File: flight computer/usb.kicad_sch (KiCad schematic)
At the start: 33 parts, among them J11 USB_C_Receptacle_USB2.0_16P, J23 USB_C_Receptacle_USB2.0_16P, J24 USB_C_Receptacle_USB2.0_16P

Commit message: tspmo
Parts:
- removed C37, C39: 4n7, Capacitor_SMD:C_0603_1608Metric, symbol Device:C
- removed C38, C40: 100n, Capacitor_SMD:C_0603_1608Metric, symbol Device:C
- removed D10, D12: PRTR5V0U2X, Package_TO_SOT_SMD:SOT-143, symbol Power_Protection:PRTR5V0U2X
- removed D11, D9: LED, LED_SMD:LED_0603_1608Metric, symbol Device:LED
- removed D27, D28: PMEG6020ER, Diode_SMD:Nexperia_CFP3_SOD-123W, symbol Diode:PMEG6020ER
- removed J23, J24: USB_C_Receptacle_USB2.0_16P, Connector_USB:USB_C_Receptacle_GCT_USB4105-xx-A_16P_TopMnt_Horizontal, symbol Connector:USB_C_Receptacle_USB2.0_16P
- removed R48, R49, R86, R96: 5k1, Resistor_SMD:R_0603_1608Metric, symbol Device:R
- removed R50, R97: 330, Resistor_SMD:R_0603_1608Metric, symbol Device:R
- removed TP14, TP15, TP16, TP17: TestPoint, TestPoint:TestPoint_Pad_1.0x1.0mm, symbol Connector:TestPoint
- added SW1, SW2: SW_SP3T, NR01103ANG13-1C:SW_NR01103ANG13-1C, symbol Switch:SW_SP3T
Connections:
- net D+ DMCU-1: now also SW1.2
- net D+ DMCU-2: now also SW1.4
- net D+ MMCU: now also SW1.1; no longer D8.2 (I/O1), J11.A6 (D+), J11.B6 (D+), TP12.1
- net D- DMCU-1: now also SW2.2
- net D- DMCU-2: now also SW2.4
- net D- MMCU: now also SW2.1; no longer D8.3 (I/O2), J11.A7 (D-), J11.B7 (D-), TP13.1
- new net: D8.3 (I/O2), J11.A7 (D-), J11.B7 (D-), SW2.3, TP13.1
- new net: D8.2 (I/O1), J11.A6 (D+), J11.B6 (D+), SW1.3, TP12.1
- no-connect marks 6 -> 2

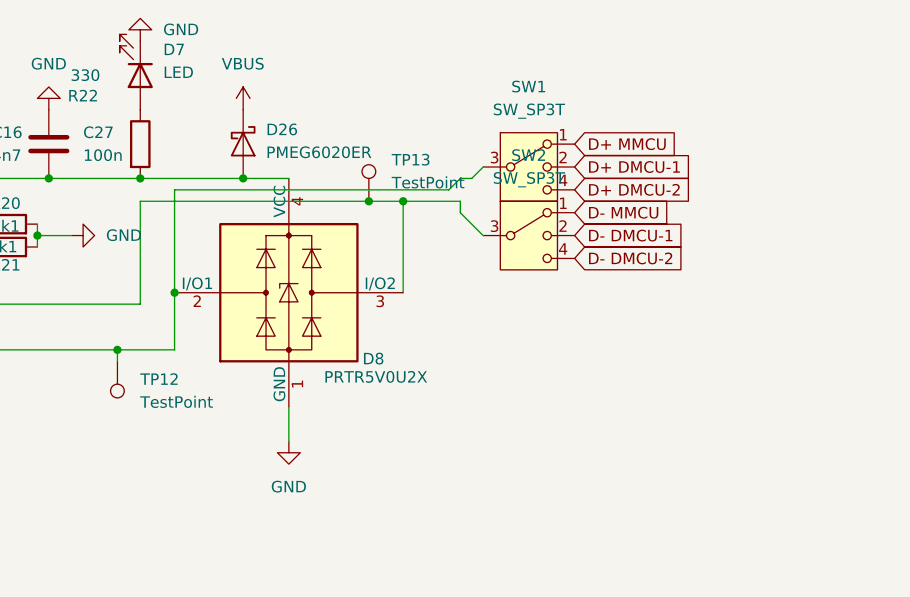
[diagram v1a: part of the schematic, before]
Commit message: started to change to bridging and PCB stiching and stuff fixes
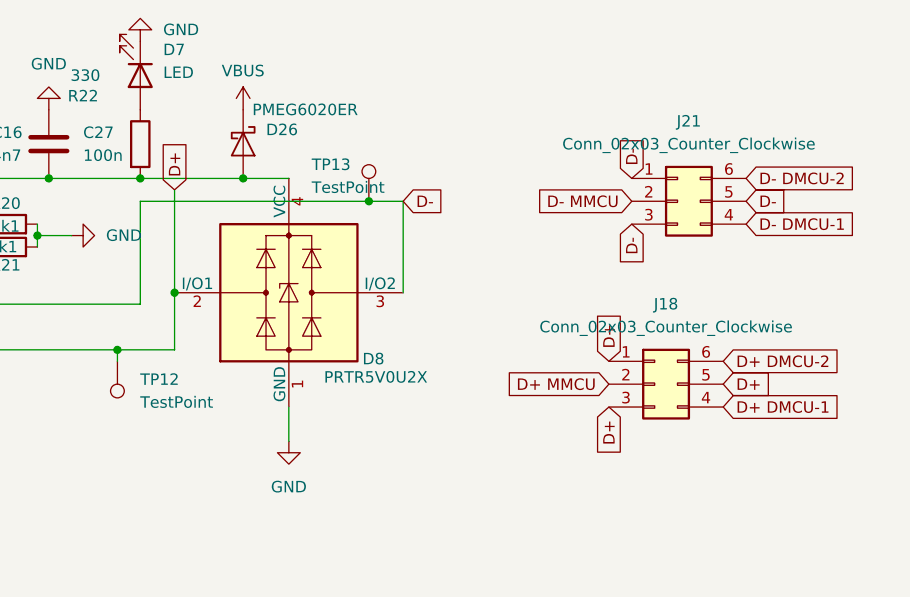
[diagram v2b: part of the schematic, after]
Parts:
- removed SW1, SW2: SW_SP3T, NR01103ANG13-1C:SW_NR01103ANG13-1C, symbol Switch:SW_SP3T
- added J18, J21: Conn_02x03_Counter_Clockwise, symbol Connector_Generic:Conn_02x03_Counter_Clockwise
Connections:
- net D+ DMCU-1: now also J18.4 (Pin_4)
- net D+ DMCU-2: now also J18.6 (Pin_6)
- net D+ MMCU: now also J18.2 (Pin_2)
- net D- DMCU-1: now also J21.4 (Pin_4)
- net D- DMCU-2: now also J21.6 (Pin_6)
- net D- MMCU: now also J21.2 (Pin_2)
- net D-: now reaches D8.3 (I/O2), J11.A7 (D-), J11.B7 (D-), TP13.1
- net D-: now also J21.1 (Pin_1), J21.3 (Pin_3), J21.5 (Pin_5)
- net D+  : now reaches D8.2 (I/O1), J11.A6 (D+), J11.B6 (D+), TP12.1
- net D+  : now also J18.1 (Pin_1), J18.3 (Pin_3), J18.5 (Pin_5)

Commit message: Wired the headers for programming 3 MCU'S + some footprint fixes and additions for photos:(
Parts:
- J18, J21: footprint (none) -> Connector_PinSocket_2.00mm:PinSocket_2x03_P2.00mm_Horizontal
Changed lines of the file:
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@@
 			)
 		)
-		(property "Footprint" ""
+		(property "Footprint" "Connector_PinSocket_2.00mm:PinSocket_2x03_P2.00mm_Horizontal"
 			(at 127 30.48 0)
 			(effects
@@
 			)
 		)
-		(property "Footprint" ""
+		(property "Footprint" "Connector_PinSocket_2.00mm:PinSocket_2x03_P2.00mm_Horizontal"
 			(at 124.46 50.8 0)
 			(effects

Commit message: Meddy, the PCB is ready for you. The proper RF is setup too on the PCB
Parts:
- added FB1: BLM18AG601SN1D, Resistor_SMD:R_0603_1608Metric, symbol Device:FerriteBead_Small
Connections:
- net GND: now also FB1.2; no longer J11.S1 (SHIELD)
- new net: FB1.1, J11.S1 (SHIELD)
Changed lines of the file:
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@@
 	(paper "A4")
+	(junction
+		(at 27.94 66.04)
+		(diameter 0)
+		(color 0 0 0 0)
+	)
 	(junction
 		(at 43.18 46.99)
@@
 	(wire
 		(pts
+			(xy 26.67 66.04) (xy 27.94 66.04)
+		)
+		(stroke
+			(width 0)
+			(type default)
+		)
+	)
+	(wire
+		(pts
 			(xy 55.88 33.02) (xy 55.88 34.29)
 		)
@@
 		(pts
 			(xy 67.31 27.94) (xy 78.74 27.94)
+		)
+		(stroke
+			(width 0)
+			(type default)
+		)
+	)
+	(wire
+		(pts
+			(xy 21.59 66.04) (xy 20.32 66.04)
 		)
 		(stroke
@@
 	(symbol
 		(lib_id "power:GND")
-		(at 20.32 66.04 0)
-		(unit 1)
-		(exclude_from_sim no)
-		(in_bom yes)
-		(on_board yes)
-		(dnp no)
-		(property "Reference" "#PWR070"
-			(at 20.32 72.39 0)
-			(effects
-				(font
-					(size 1.27 1.27)
-				)
-				(hide yes)
-			)
-		)
-		(property "Value" "GND"
-			(at 20.32 71.12 0)
-			(effects
-				(font
-					(size 1.27 1.27)
-				)
-			)
-		)
-		(property "Footprint" ""
-			(at 20.32 66.04 0)
-			(effects
-				(font
-					(size 1.27 1.27)
-				)
-				(hide yes)
-			)
-		)
-		(property "Datasheet" ""
-			(at 20.32 66.04 0)
-			(effects
-				(font
-					(size 1.27 1.27)
-				)
-				(hide yes)
-			)
-		)
-		(property "Description" "Power symbol creates a global label with name \"GND\" , ground"
-			(at 20.32 66.04 0)
-			(effects
-				(font
-					(size 1.27 1.27)
-				)
-				(hide yes)
-			)
-		)
-		(pin "1"
-		)
-		(instances
-			(project "horizon"
-				(path "/78d9c2f3-deae-418a-8c21-4820ea8fc57f/097de61a-b781-409b-916d-2a6fba459f37"
-					(reference "#PWR070")
-					(unit 1)
-				)
-			)
-		)
-	)
-	(symbol
-		(lib_id "power:GND")
 		(at 57.15 20.32 180)
 		(unit 1)
@@
 	)
 	(symbol
-		(lib_id "power:GND")
-		(at 27.94 66.04 0)
+		(lib_id "Device:FerriteBead_Small")
+		(at 24.13 66.04 90)
 		(unit 1)
 		(exclude_from_sim no)
@@
 		(on_board yes)
 		(dnp no)
-		(fields_autoplaced yes)
-		(property "Reference" "#PWR0154"
-			(at 27.94 72.39 0)
-			(effects
-				(font
-					(size 1.27 1.27)
-				)
-				(hide yes)
-			)
-		)
-		(property "Value" "GND"
-			(at 27.94 71.12 0)
-			(effects
-				(font
-					(size 1.27 1.27)
-				)
-			)
-		)
-		(property "Footprint" ""
-			(at 27.94 66.04 0)
-			(effects
-				(font
-					(size 1.27 1.27)
-				)
-				(hide yes)
-			)
-		)
-		(property "Datasheet" ""
-			(at 27.94 66.04 0)
-			(effects
-				(font
-					(size 1.27 1.27)
-				)
-				(hide yes)
-			)
-		)
-		(property "Description" "Power symbol creates a global label with name \"GND\" , ground"
-			(at 27.94 66.04 0)
-			(effects
-				(font
-					(size 1.27 1.27)
-				)
-				(hide yes)
-			)
+		(property "Reference" "FB1"
+			(at 24.13 70.104 90)
+			(effects
+				(font
+					(size 1.27 1.27)
+				)
+			)
+		)
+		(property "Value" "BLM18AG601SN1D"
+			(at 24.13 72.644 90)
+			(effects
+				(font
+					(size 1.27 1.27)
+				)
+			)
+		)
+		(property "Footprint" "Resistor_SMD:R_0603_1608Metric"
+			(at 24.13 67.818 90)
+			(effects
+				(font
+					(size 1.27 1.27)
+				)
+				(hide yes)
+			)
+		)
+		(property "Datasheet" "~"
+			(at 24.13 66.04 0)
+			(effects
+				(font
+					(size 1.27 1.27)
+				)
+				(hide yes)
+			)
+		)
+		(property "Description" "Ferrite bead, small symbol"
+			(at 24.13 66.04 0)
+			(effects
+				(font
+					(size 1.27 1.27)
+				)
+				(hide yes)
+			)
+		)
+		(property "LCSC Part" "C19330"
+			(at 24.13 66.04 0)
+			(effects
+				(font
+					(size 1.27 1.27)
+				)
+				(hide yes)
+			)
+		)
+		(pin "2"
 		)
 		(pin "1"
@@
 			(project "horizon"
 				(path "/78d9c2f3-deae-418a-8c21-4820ea8fc57f/097de61a-b781-409b-916d-2a6fba459f37"
-					(reference "#PWR0154")
+					(reference "FB1")
 					(unit 1)
 				)
@@
 					(unit 1)
 				)
+			)
+		)
+	)
+	(symbol
+		(lib_id "power:GND")
+		(at 27.94 66.04 0)
+		(unit 1)
+		(exclude_from_sim no)
+		(in_bom yes)
+		(on_board yes)
+		(dnp no)
+		(property "Reference" "#PWR033"
+			(at 27.94 72.39 0)
+			(effects
+				(font
+					(size 1.27 1.27)
+				)
+				(hide yes)
+			)
+		)
+		(property "Value" "GND"
+			(at 27.94 71.12 0)
+			(effects
+				(font
+					(size 1.27 1.27)
+				)
+			)
+		)
+		(property "Footprint" ""
+			(at 27.94 66.04 0)
+			(effects
+				(font
+					(size 1.27 1.27)
+				)
+				(hide yes)
+			)
+		)
+		(property "Datasheet" ""
+			(at 27.94 66.04 0)
+			(effects
+				(font
+					(size 1.27 1.27)
+				)
+				(hide yes)
+			)
+		)
+		(property "Description" "Power symbol creates a global label with name \"GND\" , ground"
+			(at 27.94 66.04 0)
+			(effects
+				(font
+					(size 1.27 1.27)
+				)
+				(hide yes)
+			)
+		)
+		(pin "1"
+		)
+		(instances
+			(project "horizon"
+				(path "/78d9c2f3-deae-418a-8c21-4820ea8fc57f/097de61a-b781-409b-916d-2a6fba459f37"
+					(reference "#PWR033")
+					(unit 1)
+				)

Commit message: finished power stuff
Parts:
- removed TP12, TP13: TestPoint, TestPoint:TestPoint_Pad_1.0x1.0mm, symbol Connector:TestPoint
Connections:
- net D-: now also D8.2 (I/O1); no longer D8.3 (I/O2)
- net D+   renamed D+
- net D+: now also D8.3 (I/O2); no longer D8.2 (I/O1)
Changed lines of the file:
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@@
-	)
-	(junction
-		(at 64.77 46.99)
-		(diameter 0)
-		(color 0 0 0 0)
 	)
 	(junction
@@
 	)
 	(junction
-		(at 92.71 30.48)
-		(diameter 0)
-		(color 0 0 0 0)
-	)
-	(junction
-		(at 71.12 40.64)
-		(diameter 0)
-		(color 0 0 0 0)
-	)
-	(junction
 		(at 78.74 27.94)
 		(diameter 0)
@@
 	(wire
 		(pts
+			(xy 68.58 29.21) (xy 95.25 29.21)
+		)
+		(stroke
+			(width 0)
+			(type default)
+		)
+	)
+	(wire
+		(pts
 			(xy 55.88 34.29) (xy 59.69 34.29)
 		)
@@
 	(wire
 		(pts
-			(xy 71.12 40.64) (xy 71.12 29.21)
-		)
-		(stroke
-			(width 0)
-			(type default)
-		)
-	)
-	(wire
-		(pts
-			(xy 92.71 30.48) (xy 96.52 30.48)
+			(xy 68.58 29.21) (xy 68.58 46.99)
+		)
+		(stroke
+			(width 0)
+			(type default)
+		)
+	)
+	(wire
+		(pts
+			(xy 67.31 30.48) (xy 96.52 30.48)
 		)
 		(stroke
@@
 	(wire
 		(pts
-			(xy 43.18 46.99) (xy 64.77 46.99)
-		)
-		(stroke
-			(width 0)
-			(type default)
-		)
-	)
-	(wire
-		(pts
 			(xy 43.18 27.94) (xy 46.99 27.94)
 		)
@@
 	(wire
 		(pts
-			(xy 67.31 30.48) (xy 92.71 30.48)
-		)
-		(stroke
-			(width 0)
-			(type default)
-		)
-	)
-	(wire
-		(pts
 			(xy 46.99 27.94) (xy 57.15 27.94)
 		)
@@
 	(wire
 		(pts
-			(xy 64.77 48.26) (xy 64.77 46.99)
-		)
-		(stroke
-			(width 0)
-			(type default)
-		)
-	)
-	(wire
-		(pts
-			(xy 71.12 46.99) (xy 71.12 40.64)
-		)
-		(stroke
-			(width 0)
-			(type default)
-		)
-	)
-	(wire
-		(pts
-			(xy 96.52 30.48) (xy 96.52 40.64)
-		)
-		(stroke
-			(width 0)
-			(type default)
-		)
-	)
-	(wire
-		(pts
-			(xy 64.77 46.99) (xy 71.12 46.99)
+			(xy 43.18 46.99) (xy 68.58 46.99)
 		)
 		(stroke
@@
 		(pts
 			(xy 43.18 46.99) (xy 43.18 48.26)
+		)
+		(stroke
+			(width 0)
+			(type default)
+		)
+	)
+	(wire
+		(pts
+			(xy 95.25 29.21) (xy 96.52 27.94)
 		)
 		(stroke
@@
 		)
 	)
+	(global_label "D+"
+		(shape input)
+		(at 96.52 27.94 0)
+		(fields_autoplaced yes)
+		(effects
+			(font
+				(size 1.27 1.27)
+			)
+			(justify left)
+		)
+		(property "Intersheetrefs" "${INTERSHEET_REFS}"
+			(at 102.3476 27.94 0)
+			(effects
+				(font
+					(size 1.27 1.27)
+				)
+				(justify left)
+				(hide yes)
+			)
+		)
+	)
 	(global_label "D- DMCU-1"
 		(shape input)
@@
 		)
 	)
+	(global_label "D-"
+		(shape input)
+		(at 71.12 40.64 180)
+		(fields_autoplaced yes)
+		(effects
+			(font
+				(size 1.27 1.27)
+			)
+			(justify right)
+		)
+		(property "Intersheetrefs" "${INTERSHEET_REFS}"
+			(at 65.2924 40.64 0)
+			(effects
+				(font
+					(size 1.27 1.27)
+				)
+				(justify right)
+				(hide yes)
+			)
+		)
+	)
+	(global_label "D+"
+		(shape input)
+		(at 96.52 40.64 0)
+		(fields_autoplaced yes)
+		(effects
+			(font
+				(size 1.27 1.27)
+			)
+			(justify left)
+		)
+		(property "Intersheetrefs" "${INTERSHEET_REFS}"
+			(at 102.3476 40.64 0)
+			(effects
+				(font
+					(size 1.27 1.27)
+				)
+				(justify left)
+				(hide yes)
+			)
+		)
+	)
 	(global_label "D+ DMCU-2"
 		(shape input)
@@
 		)
 	)
-	(global_label "D+  "
+	(global_label "D+"
 		(shape input)
 		(at 132.08 50.8 0)
@@
 		)
 		(property "Intersheetrefs" "${INTERSHEET_REFS}"
-			(at 139.8428 50.8 0)
+			(at 137.9076 50.8 0)
 			(effects
 				(font
@@
 		)
 	)
-	(global_label "D+  "
+	(global_label "D+"
 		(shape input)
 		(at 119.38 48.26 90)
@@
 		)
 		(property "Intersheetrefs" "${INTERSHEET_REFS}"
-			(at 119.38 40.4972 90)
+			(at 119.38 42.4324 90)
 			(effects
 				(font
@@
 		)
 	)
-	(global_label "D+  "
+	(global_label "D+"
 		(shape input)
-		(at 71.12 29.21 90)
+		(at 119.38 53.34 270)
 		(fields_autoplaced yes)
 		(effects
@@
 				(size 1.27 1.27)
 			)
-			(justify left)
+			(justify right)
 		)
 		(property "Intersheetrefs" "${INTERSHEET_REFS}"
-			(at 71.12 21.4472 90)
-			(effects
-				(font
-					(size 1.27 1.27)
-				)
-				(justify left)
-				(hide yes)
-			)
-		)
-	)
-	(global_label "D+  "
-		(shape input)
-		(at 119.38 53.34 270)
-		(fields_autoplaced yes)
-		(effects
-			(font
-				(size 1.27 1.27)
-			)
-			(justify right)
-		)
-		(property "Intersheetrefs" "${INTERSHEET_REFS}"
-			(at 119.38 61.1028 90)
+			(at 119.38 59.1676 90)
 			(effects
 				(font
@@
 	)
 	(symbol
-		(lib_id "Connector:TestPoint")
-		(at 64.77 48.26 180)
-		(unit 1)
-		(exclude_from_sim no)
-		(in_bom yes)
-		(on_board yes)
-		(dnp no)
-		(fields_autoplaced yes)
-		(property "Reference" "TP12"
-			(at 67.31 50.2919 0)
-			(effects
-				(font
-					(size 1.27 1.27)
-				)
-				(justify right)
-			)
-		)
-		(property "Value" "TestPoint"
-			(at 67.31 52.8319 0)
-			(effects
-				(font
-					(size 1.27 1.27)
-				)
-				(justify right)
-			)
-		)
-		(property "Footprint" "TestPoint:TestPoint_Pad_1.0x1.0mm"
-			(at 59.69 48.26 0)
-			(effects
-				(font
-					(size 1.27 1.27)
-				)
-				(hide yes)
-			)
-		)
-		(property "Datasheet" "~"
-			(at 59.69 48.26 0)
-			(effects
-				(font
-					(size 1.27 1.27)
-				)
-				(hide yes)
-			)
-		)
-		(property "Description" "test point"
-			(at 64.77 48.26 0)
-			(effects
-				(font
-					(size 1.27 1.27)
-				)
-				(hide yes)
-			)
-		)
-		(pin "1"
-		)
-		(instances
-			(project "horizon"
-				(path "/78d9c2f3-deae-418a-8c21-4820ea8fc57f/097de61a-b781-409b-916d-2a6fba459f37"
-					(reference "TP12")
-					(unit 1)
-				)
-			)
-		)
-	)
-	(symbol
 		(lib_id "Device:R")
 		(at 52.07 33.02 90)
@@
 					(unit 1)
 				)
-			)
-		)
-	)
-	(symbol
-		(lib_id "Connector:TestPoint")
-		(at 92.71 30.48 0)
-		(unit 1)
-		(exclude_from_sim no)
-		(in_bom yes)
-		(on_board yes)
-		(dnp no)
-		(property "Reference" "TP13"
-			(at 86.36 26.416 0)
-			(effects
-				(font
-					(size 1.27 1.27)
-				)
-				(justify left)
-			)
-		)
-		(property "Value" "TestPoint"
-			(at 86.36 28.956 0)
-			(effects
-				(font
-					(size 1.27 1.27)
-				)
-				(justify left)
-			)
-		)
-		(property "Footprint" "TestPoint:TestPoint_Pad_1.0x1.0mm"
-			(at 97.79 30.48 0)
-			(effects
-				(font
-					(size 1.27 1.27)
-				)
-				(hide yes)
-			)
-		)
-		(property "Datasheet" "~"
-			(at 97.79 30.48 0)
-			(effects
-				(font
-					(size 1.27 1.27)
-				)
-				(hide yes)
-			)
-		)
-		(property "Description" "test point"
-			(at 92.71 30.48 0)
-			(effects
-				(font
-					(size 1.27 1.27)
-				)
-				(hide yes)
-			)
-		)
-		(pin "1"
-		)
-		(instances
-			(project "horizon"
-				(path "/78d9c2f3-deae-418a-8c21-4820ea8fc57f/097de61a-b781-409b-916d-2a6fba459f37"
-					(reference "TP13")
-					(unit 1)
-				)

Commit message: wiirng
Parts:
- J18, J21: footprint Connector_PinSocket_2.00mm:PinSocket_2x03_P2.00mm_Horizontal -> Connector_PinHeader_1.00mm:PinHeader_2x03_P1.00mm_Vertical
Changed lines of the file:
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@@
 			)
 		)
-		(property "Footprint" "Connector_PinSocket_2.00mm:PinSocket_2x03_P2.00mm_Horizontal"
+		(property "Footprint" "Connector_PinHeader_1.00mm:PinHeader_2x03_P1.00mm_Vertical"
 			(at 127 30.48 0)
 			(effects
@@
 			)
 		)
-		(property "Footprint" "Connector_PinSocket_2.00mm:PinSocket_2x03_P2.00mm_Horizontal"
+		(property "Footprint" "Connector_PinHeader_1.00mm:PinHeader_2x03_P1.00mm_Vertical"
 			(at 124.46 50.8 0)
 			(effects

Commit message: started newest layout + wiring
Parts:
- removed FB1: BLM18AG601SN1D, Resistor_SMD:R_0603_1608Metric, symbol Device:FerriteBead_Small
- J18, J21: footprint Connector_PinHeader_1.00mm:PinHeader_2x03_P1.00mm_Vertical -> Connector_PinHeader_2.54mm:PinHeader_2x03_P2.54mm_Vertical
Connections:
- net GND: now also J11.S1 (SHIELD)
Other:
- moved on the sheet: D8
